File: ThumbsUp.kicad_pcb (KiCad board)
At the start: 2 copper layers, 250.8 x 270.5 mm, 170 parts, among them IC1 RP2040, IC2 W25Q128JVSIM, IC3 RP2040, IC4 W25Q128JVSIM, J1 Conn_01x04_Male, J10 Raiser_Male, J11 Raiser_Female, J12 Raiser_Male, J13 Raiser_Female, J14 Raiser_Male, J15 Raiser_Female, J16 Raiser_Male, J17 Raiser_Female, J18 Raiser_Male, J19 Raiser_Female, J2 Conn_01x04_Male, J20 Conn_01x04_Female, J21 Conn_01x04_Female, J22 Conn_01x04_Female, J23 Conn_01x04_Female, J24 Conn_01x04_Male, J25 Conn_01x04_Male, J26 Conn_01x04_Male, J27 Conn_01x04_Male, J28 Conn_01x04_Female, J29 Conn_01x04_Female, J3 Conn_01x04_Female, J30 Conn_01x04_Female, J31 Conn_01x04_Female, J32 USB_C_Receptacle_USB2.0, J33 Raiser_Male, J34 Raiser_Female, J35 Raiser_Male, J36 STX-3501-3N, J37 USB_C_Receptacle_USB2.0, J38 Raiser_Female, J39 Raiser_Male, J4 Conn_01x04_Male, J40 Raiser_Female, J41 Raiser_Male, J42 Raiser_Female, J43 Raiser_Male, J44 Raiser_Female, J45 Raiser_Male, J46 STX-3501-3N, J47 Raiser_Female, J48 Raiser_Male, J49 Raiser_Female, J5 Conn_01x04_Female, J50 Raiser_Male, J51 Raiser_Female, J52 Raiser_Male, J6 Conn_01x04_Male, J7 Conn_01x04_Male, J8 Conn_01x04_Male, J9 Raiser_Female, U1 AMS1117-3.3_SOT223, U2 AMS1117-3.3_SOT223, Y1 ABLS-12.000MHZ-B4-T, Y2 ABLS-12.000MHZ-B4-T

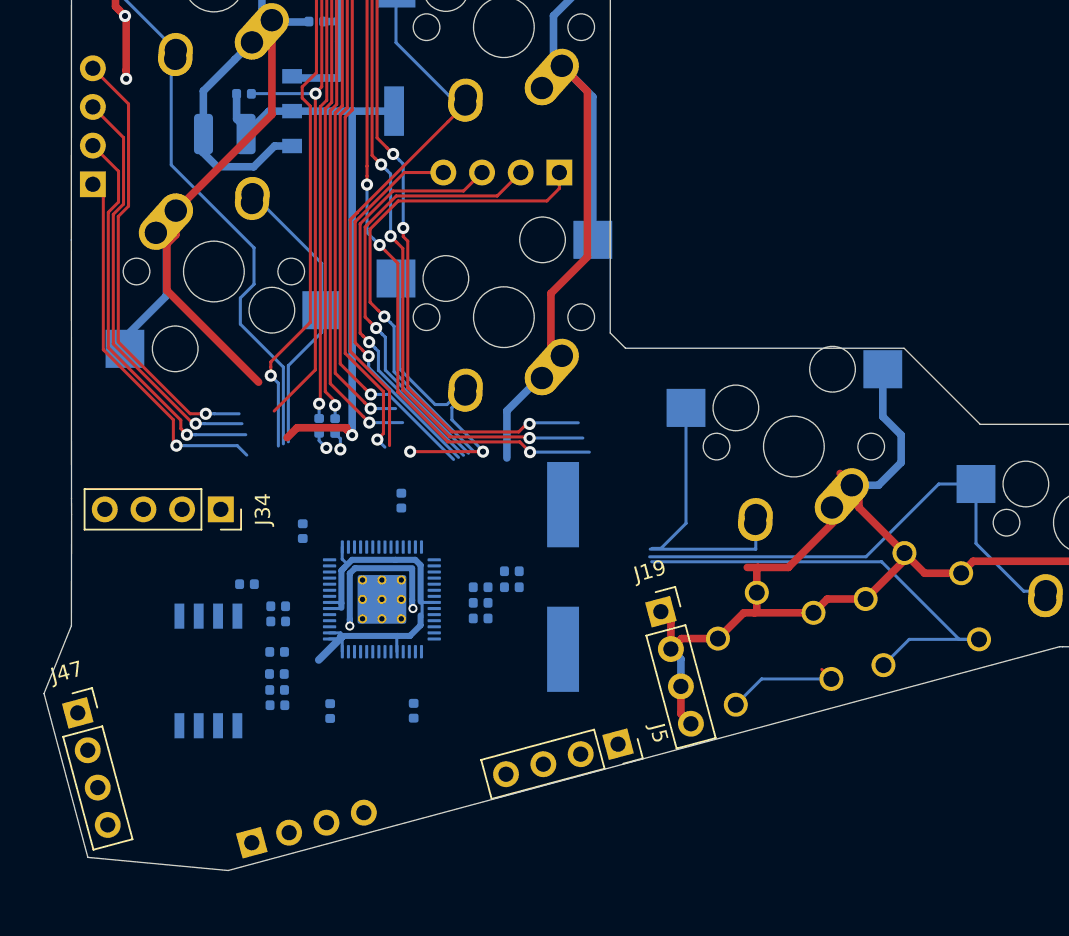
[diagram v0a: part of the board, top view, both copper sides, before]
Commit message: Wired both RP2040s
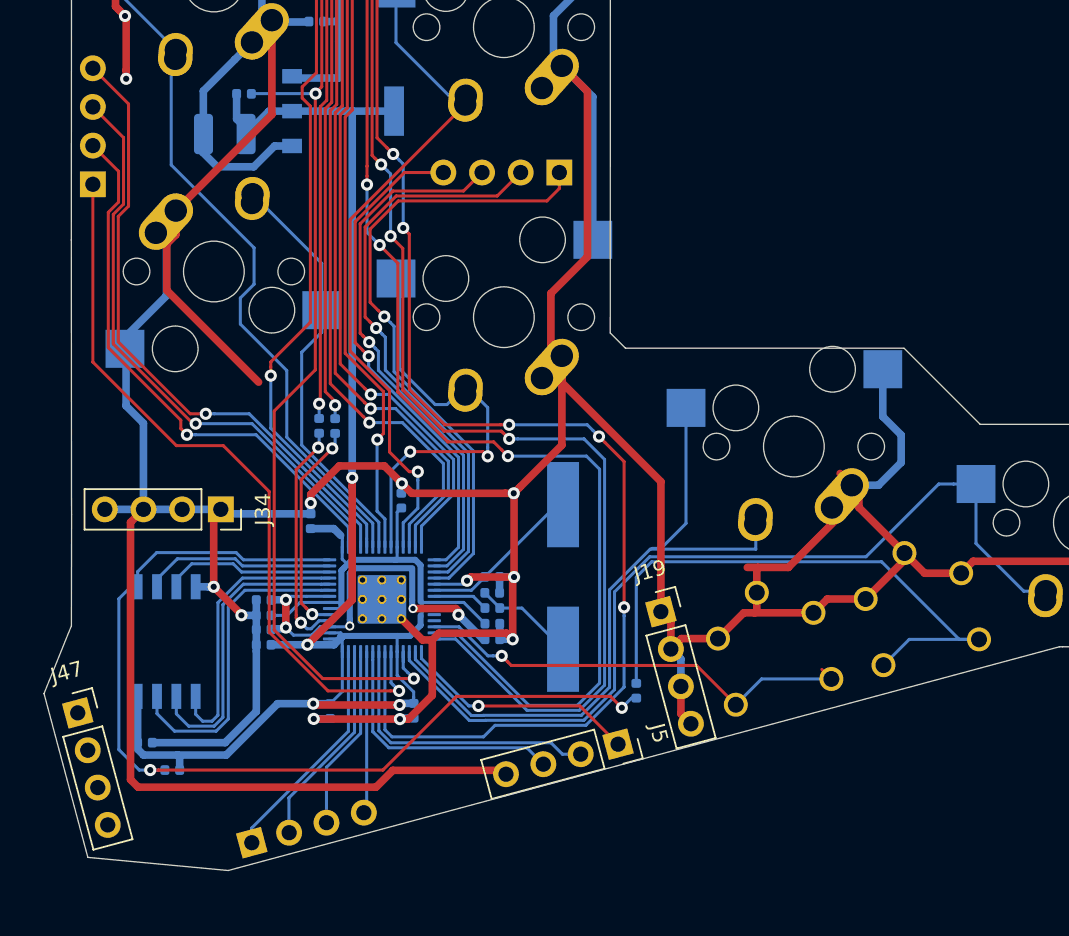
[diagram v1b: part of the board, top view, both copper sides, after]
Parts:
- moved R12 23.6 mm to (191.1, 463.0), turned to 270 degrees
- moved C19 12.4 mm to (158.8, 466.4)
- moved R13 8.66 mm to (160.6, 468.2)
- moved C25 3.95 mm to (166.6, 458.1)
- moved C24 3.52 mm to (166.6, 457.0)
- moved IC4 3.35 mm to (160.3, 459.8), turned to 270 degrees
- moved C20 1.80 mm to (166.6, 460.0)
- moved C26 1.80 mm to (166.6, 459.0)
- moved C28 1.57 mm to (181.7, 459.6)
- moved C29 1.57 mm to (181.7, 458.6)
- moved R16 1.57 mm to (181.7, 457.6)
- moved C21 1.34 mm to (181.6, 455.5)
- moved C22 1.34 mm to (181.6, 456.6)
- moved C27 0.83 mm to (169.7, 451.9)
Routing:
- net L-BASE: track 842.4 -> 1015.5 mm, vias 14 -> 24
- net RQSPI_SSN: track 0.00 -> 63.9 mm, vias 0 -> 2
- net +3V3: track 171.1 -> 231.6 mm, vias 5 -> 8
- net K_7: track 96.6 -> 137.3 mm, vias 3 -> 5
- net K_8: track 75.6 -> 106.3 mm
- net +1V1: track 27.2 -> 56.4 mm, vias 4 -> 9
- net K_9: track 74.7 -> 103.3 mm
- net R-TIP: track 65.4 -> 93.0 mm, vias 1 -> 2
- net K_MNU: track 33.2 -> 59.4 mm
- net K_RALT: track 19.1 -> 44.8 mm
- net K_BSPC: track 24.3 -> 48.9 mm
- net Net-(IC3-Pad26): track 7.86 -> 29.8 mm, vias 0 -> 1
- net RQSPI_SD3: track 0.00 -> 21.1 mm
- net RQSPI_SCLK: track 0.00 -> 19.7 mm
- net K_LWR: track 0.00 -> 19.1 mm
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
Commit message: Wired both RP2040s
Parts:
- removed MX57: SwThL, MX_Alps_Hybrid:MX-1U-NoLED_HotSwap
- removed MX58: SwThR, MX_Alps_Hybrid:MX-1U-NoLED_HotSwap
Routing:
- net L-BASE: track 1015.5 -> 985.4 mm, vias 24 -> 22

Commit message: Wired both RP2040s
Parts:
- MX1, MX10, MX11, MX12, MX13, MX14, MX15, MX16, MX17, MX18, MX19, MX2, MX20, MX21, MX22, MX23, MX24, MX25, MX26, MX27, MX28, MX29, MX3, MX30, MX31, MX32, MX33, MX34, MX35, MX36, MX37, MX38, MX39, MX4, MX40, MX41, MX42, MX43, MX44, MX45, MX46, MX47, MX48, MX49, MX5, MX50, MX51, MX52, MX53, MX54, MX55, MX56, MX6, MX7, MX8, MX9: footprint MX_Alps_Hybrid:MX-1U-NoLED_HotSwap -> keyswitches:MX-GLP2-HotSwap
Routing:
- net (no net): track 0.00 -> 0.76 mm
- net K_R: track 68.9 -> 68.3 mm

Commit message: Layed out tracks on L2
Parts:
- added MX57: SwThL, keyswitches:MX-GLP2-HotSwap, F.Cu at (133.4, 316.5)
- added MX58: SwThR, keyswitches:MX-GLP2-HotSwap, F.Cu at (153.6, 316.5)
- J36, J46: value STX-3501-3N -> PJ-3200B; footprint STX-3501-3N:STX35013N -> random-keyboard-parts:PJ-3200B-4A
- moved C9 45.6 mm to (125.1, 376.7)
- moved J36 23.9 mm to (129.3, 367.6), turned to 180 degrees
- moved J46 19.0 mm to (154.8, 367.3), turned to 0 degrees
- moved U1 19.0 mm to (112.7, 407.8)
- moved C11 14.6 mm to (109.3, 448.5), turned to 270 degrees
- moved R9 11.7 mm to (106.9, 372.7), turned to 270 degrees
- moved R8 10.8 mm to (107.9, 372.7), turned to 90 degrees
- moved J32 4.28 mm to (111.6, 367.9)
- moved J37 4.21 mm to (172.4, 367.8)
- moved R1 3.61 mm to (111.8, 449.8)
- moved R2 3.61 mm to (112.8, 449.8)
- moved F1 1.34 mm to (111.6, 379.8), turned to 180 degrees
- turned MX10 to 0 degrees
- turned MX14 to 0 degrees
- turned MX19 to 180 degrees
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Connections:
- J1 pad 1: K_WIN -> (no net)
- J1 pad 3: (no net) -> L-BASE
- J1 pad 4: (no net) -> L-BASE
- J36 pad 2: L-TIP -> L-RING1
- J36 pad 3: L-RING1 -> L-TIP
- J39 pad 1: K_5 -> (no net)
- J46 pad 2: R-TIP -> L-RING1
- J46 pad 3: L-RING1 -> R-TIP
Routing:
- net L-BASE: track 985.4 -> 911.6 mm, vias 22 -> 23
- net (no net): track 0.76 -> 34.1 mm
- net L-TIP: track 93.8 -> 122.6 mm, vias 1 -> 2
- net K_4: track 123.2 -> 102.2 mm, vias 1 -> 2
- net K_T: track 85.5 -> 69.6 mm, vias 1 -> 2
- net +3V3: track 231.6 -> 246.7 mm
- net K_LALT: track 46.2 -> 33.1 mm
- net K_WIN: track 65.7 -> 52.6 mm
- net L-RING1: track 108.3 -> 118.7 mm
- net K_B: track 36.5 -> 28.3 mm
- net K_5: track 118.2 -> 111.4 mm, vias 1 -> 3
- net K_F: track 59.8 -> 53.3 mm, vias 1 -> 2
- net Net-(J32-PadB5): track 5.98 -> 11.5 mm, vias 0 -> 2
- net D-: track 78.5 -> 83.5 mm
- net +5VA: track 32.6 -> 36.3 mm
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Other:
- outline, holes or cut-outs redrawn
- board text added: "u/ak66666 ThumbsUp! v7 2023-08-30"
- board text removed: "u/AK66666 ThumbsUp! v4 MX 2023-05-15"

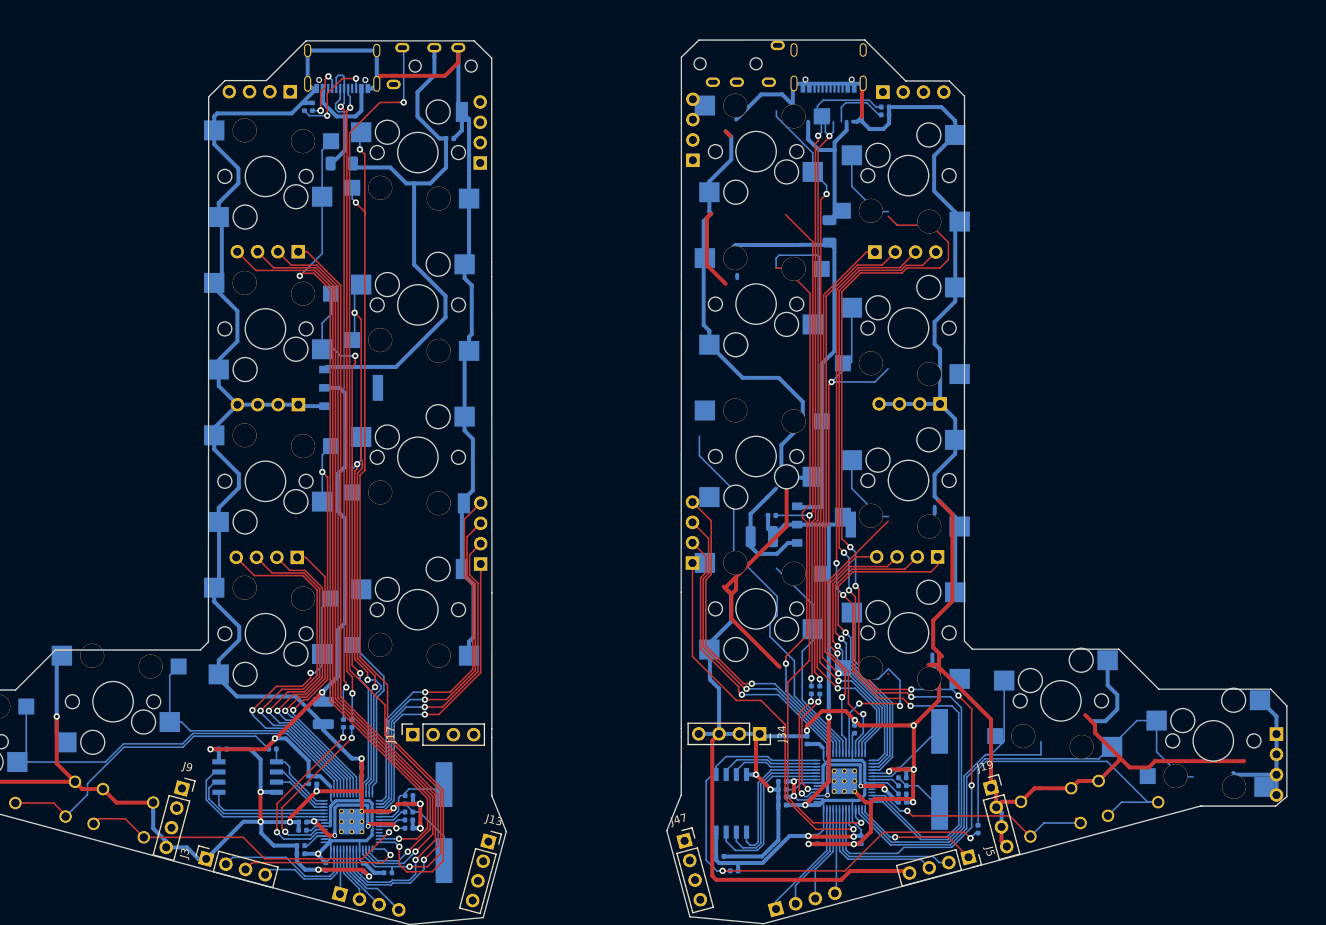
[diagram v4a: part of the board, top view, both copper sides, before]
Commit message: Layed out tracks on R2
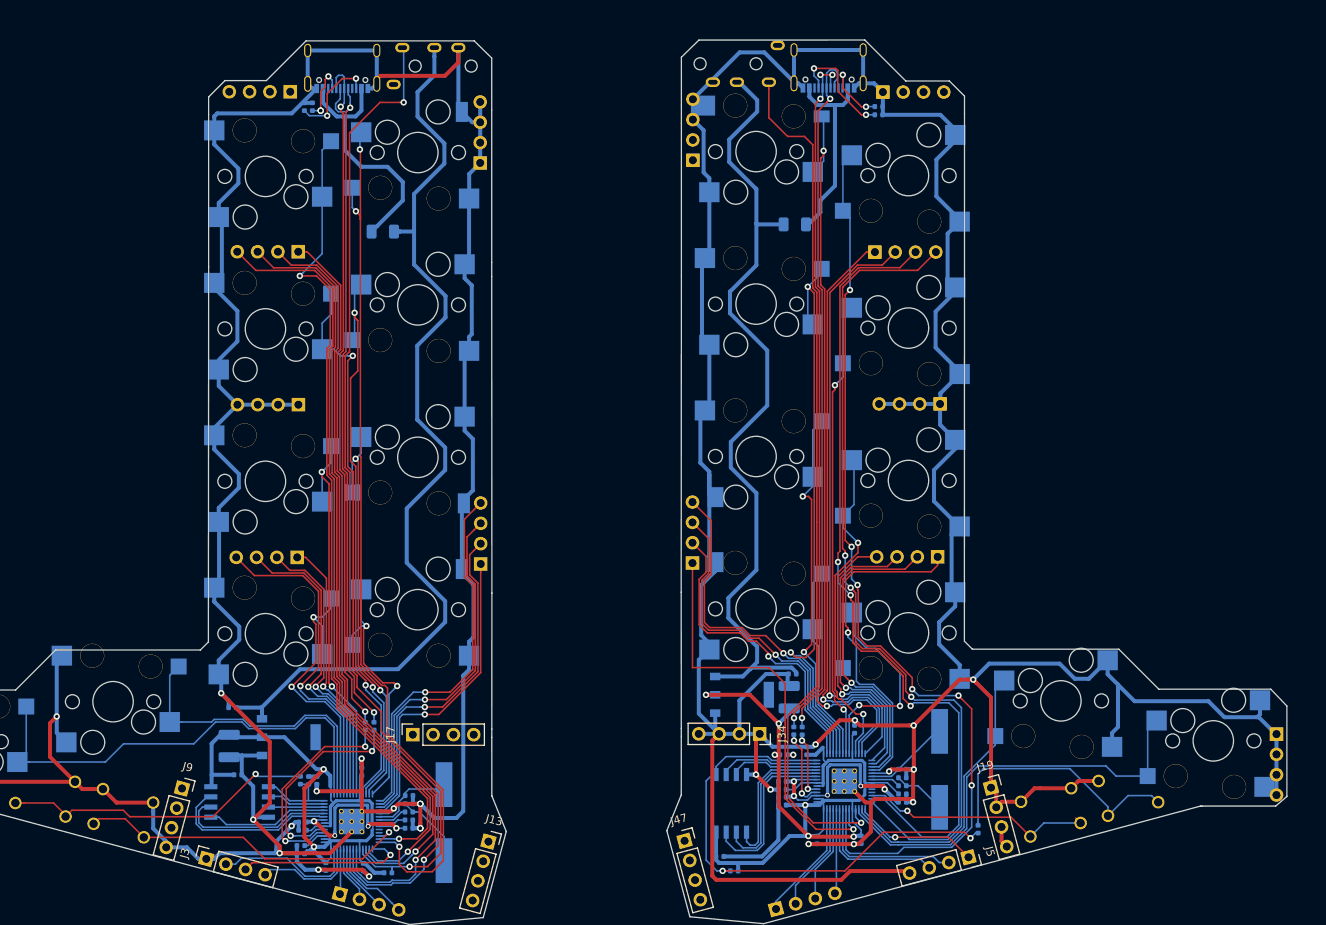
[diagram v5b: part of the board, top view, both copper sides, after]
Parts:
- moved C9 76.2 mm to (97.9, 447.8), turned to 180 degrees
- moved U1 44.4 mm to (105.0, 451.5)
- moved R5 29.9 mm to (166.8, 453.7)
- moved C8 24.7 mm to (167.9, 443.6)
- moved U2 23.6 mm to (161.6, 446.2)
- moved C18 20.4 mm to (167.5, 446.5), turned to 90 degrees
- moved C11 12.5 mm to (97.5, 452.6)
- moved F1 9.93 mm to (116.7, 388.3)
- moved R15 5.55 mm to (168.1, 450.7)
- moved R14 5.55 mm to (169.1, 450.7)
- moved R3 5.23 mm to (106.4, 456.9), turned to 270 degrees
- moved F2 4.41 mm to (168.2, 387.4), turned to 0 degrees
- moved C10 3.74 mm to (98.6, 456.2)
- moved IC2 3.27 mm to (98.8, 459.6)
- moved R2 2.78 mm to (115.6, 450.1)
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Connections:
- J39 pad 1: (no net) -> L-BASE
- J39 pad 2: (no net) -> L-BASE
- J39 pad 3: (no net) -> L-BASE
- J39 pad 4: (no net) -> L-BASE
- J41 pad 3: (no net) -> L-BASE
- J41 pad 4: (no net) -> L-BASE
- J52 pad 1: (no net) -> L-BASE
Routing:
- net L-RING1: track 118.7 -> 220.2 mm
- net +3V3: track 246.7 -> 201.1 mm
- net L-BASE: track 911.6 -> 947.4 mm, vias 23 -> 25
- net (no net): track 34.1 -> 0.88 mm
- net +5VA: track 36.3 -> 55.8 mm
- net K_7: track 137.3 -> 117.9 mm, vias 5 -> 6
- net R-TIP: track 93.0 -> 109.2 mm
- net RD+: track 73.8 -> 87.6 mm
- net RD-: track 75.2 -> 86.8 mm, vias 2 -> 4
- net K_Y: track 83.1 -> 72.6 mm, vias 1 -> 2
- net K_U: track 66.3 -> 57.4 mm
- net K_RALT: track 44.8 -> 36.0 mm
- net K_WIN: track 52.6 -> 58.8 mm
- net Net-(IC3-Pad47): track 14.2 -> 8.25 mm
- net Net-(IC3-Pad46): track 15.5 -> 10.0 mm
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
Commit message: Layed out tracks on R2
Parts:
- moved U2 0.41 mm to (161.2, 446.1), turned to 180 degrees
- turned C8 to 0 degrees
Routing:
- net +3V3: track 201.1 -> 193.4 mm, vias 8 -> 7
- net L-RING1: track 220.2 -> 222.5 mm
- net K_6: track 92.0 -> 90.5 mm
- net K_DEL: track 73.7 -> 72.3 mm
- net K_7: track 117.9 -> 119.2 mm
- net K_0: track 74.9 -> 73.9 mm
- net K_Y: track 72.6 -> 71.8 mm
- net K_8: track 105.0 -> 105.7 mm
- net K_COMM: track 42.1 -> 41.4 mm
- net K_DOT: track 39.0 -> 38.3 mm
- net K_SLASH: track 36.6 -> 36.0 mm

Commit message: Layed out tracks on the bottom level havles
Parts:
- turned MX3 to 0 degrees
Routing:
- net Net-(J44-Pad4): track 76.7 -> 59.7 mm, vias 0 -> 1
- net Net-(J23-Pad1): track 106.9 -> 90.2 mm, vias 0 -> 1
- net Net-(J23-Pad3): track 56.8 -> 41.2 mm, vias 0 -> 1
- net Net-(J31-Pad4): track 102.1 -> 91.0 mm, vias 0 -> 1
- net Net-(J29-Pad1): track 61.5 -> 51.5 mm, vias 0 -> 1
- net Net-(J31-Pad1): track 24.7 -> 15.1 mm, vias 0 -> 1
- net Net-(J15-Pad3): track 106.3 -> 96.9 mm, vias 0 -> 1
- net Net-(J23-Pad2): track 74.0 -> 65.0 mm, vias 0 -> 1
- net Net-(J23-Pad4): track 23.5 -> 14.9 mm, vias 0 -> 1
- net Net-(J21-Pad1): track 41.1 -> 32.6 mm, vias 0 -> 1
- net Net-(J15-Pad1): track 154.5 -> 146.1 mm, vias 0 -> 1
- net Net-(J44-Pad3): track 87.4 -> 79.0 mm, vias 0 -> 1
- net Net-(J15-Pad4): track 105.8 -> 97.4 mm, vias 0 -> 1
- net Net-(J31-Pad3): track 72.2 -> 64.0 mm, vias 0 -> 1
- net Net-(J21-Pad2): track 53.5 -> 45.7 mm, vias 0 -> 1
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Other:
- outline, holes or cut-outs redrawn

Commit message: Adding the 3key thumbclusters
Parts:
- added J10: Raiser_Male, Connector_PinHeader_2.54mm:PinHeader_1x04_P2.54mm_Vertical, B.Cu at (-129.0, 461.6)
- added J10: Raiser_Male, Connector_PinHeader_2.54mm:PinHeader_1x04_P2.54mm_Vertical, B.Cu at (-98.3, 395.4)
- added J10: Raiser_Male, Connector_PinHeader_2.54mm:PinHeader_1x04_P2.54mm_Vertical, B.Cu at (-87.5, 342.2)
- added J14: Raiser_Male, Connector_PinHeader_2.54mm:PinHeader_1x04_P2.54mm_Vertical, B.Cu at (-90.2, 458.1)
- added J14: Raiser_Male, Connector_PinHeader_2.54mm:PinHeader_1x04_P2.54mm_Vertical, B.Cu at (-59.6, 391.9)
- added J14: Raiser_Male, Connector_PinHeader_2.54mm:PinHeader_1x04_P2.54mm_Vertical, B.Cu at (-48.8, 338.7)
- added J18: Raiser_Male, Connector_PinHeader_2.54mm:PinHeader_1x04_P2.54mm_Vertical, B.Cu at (-102.8, 447.6)
- added J18: Raiser_Male, Connector_PinHeader_2.54mm:PinHeader_1x04_P2.54mm_Vertical, B.Cu at (-72.2, 381.4)
- added J18: Raiser_Male, Connector_PinHeader_2.54mm:PinHeader_1x04_P2.54mm_Vertical, B.Cu at (-61.4, 328.2)
- added J33: Raiser_Male, Connector_PinHeader_2.54mm:PinHeader_1x04_P2.54mm_Vertical, B.Cu at (2.85, 461.5)
- added J33: Raiser_Male, Connector_PinHeader_2.54mm:PinHeader_1x04_P2.54mm_Vertical, B.Cu at (3.49, 395.3)
- added J33: Raiser_Male, Connector_PinHeader_2.54mm:PinHeader_1x04_P2.54mm_Vertical, B.Cu at (-4.68, 342.1)
- added J35: Raiser_Male, Connector_PinHeader_2.54mm:PinHeader_1x04_P2.54mm_Vertical, B.Cu at (-23.3, 447.5)
- added J35: Raiser_Male, Connector_PinHeader_2.54mm:PinHeader_1x04_P2.54mm_Vertical, B.Cu at (-22.7, 381.3)
- added J35: Raiser_Male, Connector_PinHeader_2.54mm:PinHeader_1x04_P2.54mm_Vertical, B.Cu at (-30.9, 328.2)
- added J4: Conn_01x04_Male, Connector_PinHeader_2.54mm:PinHeader_1x04_P2.54mm_Vertical, B.Cu at (-123.8, 469.3)
- added J4: Conn_01x04_Male, Connector_PinHeader_2.54mm:PinHeader_1x04_P2.54mm_Vertical, B.Cu at (-93.1, 403.1)
- added J48: Raiser_Male, Connector_PinHeader_2.54mm:PinHeader_1x04_P2.54mm_Vertical, B.Cu at (-35.9, 458.0)
- added J48: Raiser_Male, Connector_PinHeader_2.54mm:PinHeader_1x04_P2.54mm_Vertical, B.Cu at (-35.2, 391.8)
- added J48: Raiser_Male, Connector_PinHeader_2.54mm:PinHeader_1x04_P2.54mm_Vertical, B.Cu at (-43.4, 338.7)
- added J55: Conn_01x04_Male, Connector_PinHeader_2.54mm:PinHeader_1x04_P2.54mm_Vertical, B.Cu at (-82.3, 349.9)
- added J6: Conn_01x04_Male, Connector_PinHeader_2.54mm:PinHeader_1x04_P2.54mm_Vertical, B.Cu at (-2.12, 469.1)
- added J6: Conn_01x04_Male, Connector_PinHeader_2.54mm:PinHeader_1x04_P2.54mm_Vertical, B.Cu at (-1.48, 403.0)
- added J6: Conn_01x04_Male, Connector_PinHeader_2.54mm:PinHeader_1x04_P2.54mm_Vertical, B.Cu at (-9.65, 349.8)
- added MX18: SwLMOD, keyswitches:MX-GLP2-HotSwap, F.Cu at (-100.8, 459.5)
- added MX18: SwLMOD, keyswitches:MX-GLP2-HotSwap, F.Cu at (-70.2, 393.3)
- added MX18: SwLMOD, keyswitches:MX-GLP2-HotSwap, F.Cu at (-59.4, 337.0)
- added MX22: SwLSHFT, keyswitches:MX-GLP2-HotSwap, F.Cu at (-119.9, 459.5)
- added MX22: SwLSHFT, keyswitches:MX-GLP2-HotSwap, F.Cu at (-89.3, 393.3)
- added MX22: SwLSHFT, keyswitches:MX-GLP2-HotSwap, F.Cu at (-78.5, 340.1)
- added MX26: SwRSHFT, keyswitches:MX-GLP2-HotSwap, F.Cu at (-6.23, 459.5)
- added MX26: SwRSHFT, keyswitches:MX-GLP2-HotSwap, F.Cu at (-5.55, 393.3)
- added MX26: SwRSHFT, keyswitches:MX-GLP2-HotSwap, F.Cu at (-13.6, 340.2)
- added MX30: SwRMOD, keyswitches:MX-GLP2-HotSwap, F.Cu at (-25.3, 459.5)
- added MX30: SwRMOD, keyswitches:MX-GLP2-HotSwap, F.Cu at (-24.6, 393.3)
- added MX30: SwRMOD, keyswitches:MX-GLP2-HotSwap, F.Cu at (-32.7, 337.0)
- added MX57: SwThL, keyswitches:MX-GLP2-HotSwap, F.Cu at (-81.8, 466.2)
- added MX57: SwThL, keyswitches:MX-GLP2-HotSwap, F.Cu at (-108.3, 408.8)
- added MX58: SwThR, keyswitches:MX-GLP2-HotSwap, F.Cu at (-44.4, 466.2)
- added MX58: SwThR, keyswitches:MX-GLP2-HotSwap, F.Cu at (13.5, 408.8)
- moved MX57 196.8 mm to (-59.4, 356.0)
- moved MX58 190.4 mm to (-32.7, 356.0)
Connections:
- J10 pad 1: (no net) -> Net-(J10-Pad1)
- J10 pad 2: (no net) -> Net-(J10-Pad2)
- J10 pad 3: (no net) -> Net-(J10-Pad3)
- J10 pad 4: (no net) -> Net-(J10-Pad4)
- J14 pad 1: (no net) -> Net-(J14-Pad1)
- J14 pad 2: (no net) -> Net-(J14-Pad2)
- J14 pad 3: (no net) -> Net-(J14-Pad3)
- J14 pad 4: (no net) -> Net-(J14-Pad4)
- J18 pad 1: (no net) -> Net-(J18-Pad1)
- J18 pad 2: (no net) -> Net-(J18-Pad2)
- J18 pad 3: (no net) -> Net-(J18-Pad3)
- J18 pad 4: (no net) -> Net-(J18-Pad4)
- J33 pad 1: (no net) -> Net-(J33-Pad1)
- J33 pad 2: (no net) -> Net-(J33-Pad2)
- J33 pad 3: (no net) -> Net-(J33-Pad3)
- J33 pad 4: (no net) -> Net-(J33-Pad4)
- J35 pad 1: (no net) -> Net-(J35-Pad1)
- J35 pad 2: (no net) -> Net-(J35-Pad2)
- J35 pad 3: (no net) -> Net-(J35-Pad3)
- J35 pad 4: (no net) -> Net-(J35-Pad4)
- J48 pad 1: (no net) -> Net-(J48-Pad1)
- J48 pad 2: (no net) -> Net-(J48-Pad2)
- J48 pad 3: (no net) -> Net-(J48-Pad3)
- J48 pad 4: (no net) -> Net-(J48-Pad4)
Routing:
- net Net-(J4-Pad1): track 48.2 -> 224.1 mm, vias 0 -> 2
- net Net-(J6-Pad4): track 47.1 -> 217.6 mm
- net Net-(J6-Pad2): track 41.7 -> 166.5 mm, vias 1 -> 4
- net Net-(J4-Pad4): track 34.4 -> 125.7 mm, vias 0 -> 1
- net Net-(J4-Pad2): track 23.6 -> 94.2 mm, vias 1 -> 4
- net Net-(J6-Pad3): track 18.9 -> 76.8 mm, vias 1 -> 4
- net Net-(J4-Pad3): track 0.00 -> 36.4 mm
- net Net-(J6-Pad1): track 0.00 -> 25.4 mm, vias 0 -> 2
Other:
- board size 250.8 x 270.5 mm -> 395.5 x 277.7 mm
